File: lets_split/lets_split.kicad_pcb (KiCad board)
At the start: 2 copper layers, 113 x 82 mm, 83 parts, among them J2 CONN_01X04, P1 USB-rewire, P2 USB_OTG, P3 WS2812-Strip, SW1 SW_PUSH, SW10 SW_PUSH, SW11 SW_PUSH, SW12 SW_PUSH, SW13 SW_PUSH, SW14 SW_PUSH, SW15 SW_PUSH, SW16 SW_PUSH, SW17 SW_PUSH, SW18 SW_PUSH, SW19 SW_PUSH, SW2 SW_PUSH, SW20 SW_PUSH, SW21 SW_PUSH, SW22 SW_PUSH, SW23 SW_PUSH, SW24 SW_PUSH, SW3 SW_PUSH, SW4 SW_PUSH, SW5 SW_PUSH, SW6 SW_PUSH, SW7 SW_PUSH, SW8 SW_PUSH, SW9 SW_PUSH, U1 ArduinoProMicro

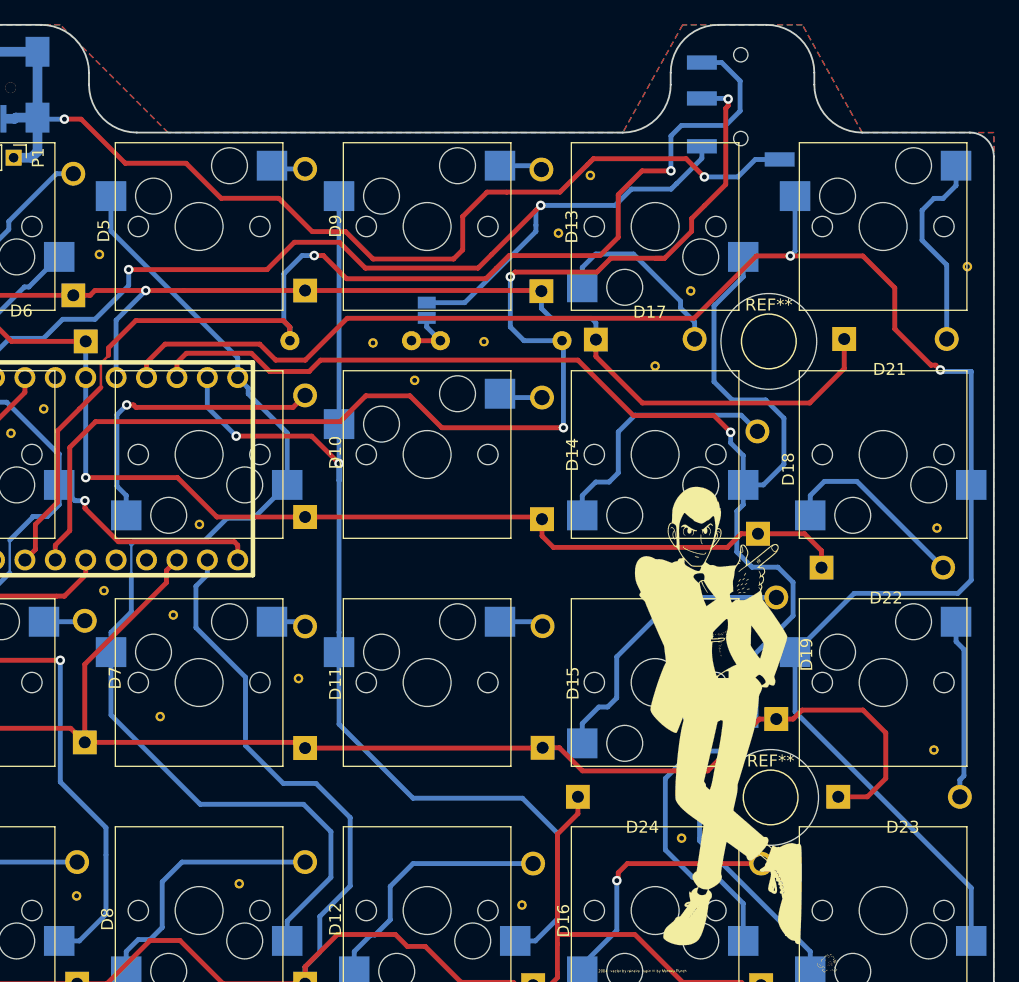
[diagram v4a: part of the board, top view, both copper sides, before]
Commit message: Changed to actually aquireable TRRS connector
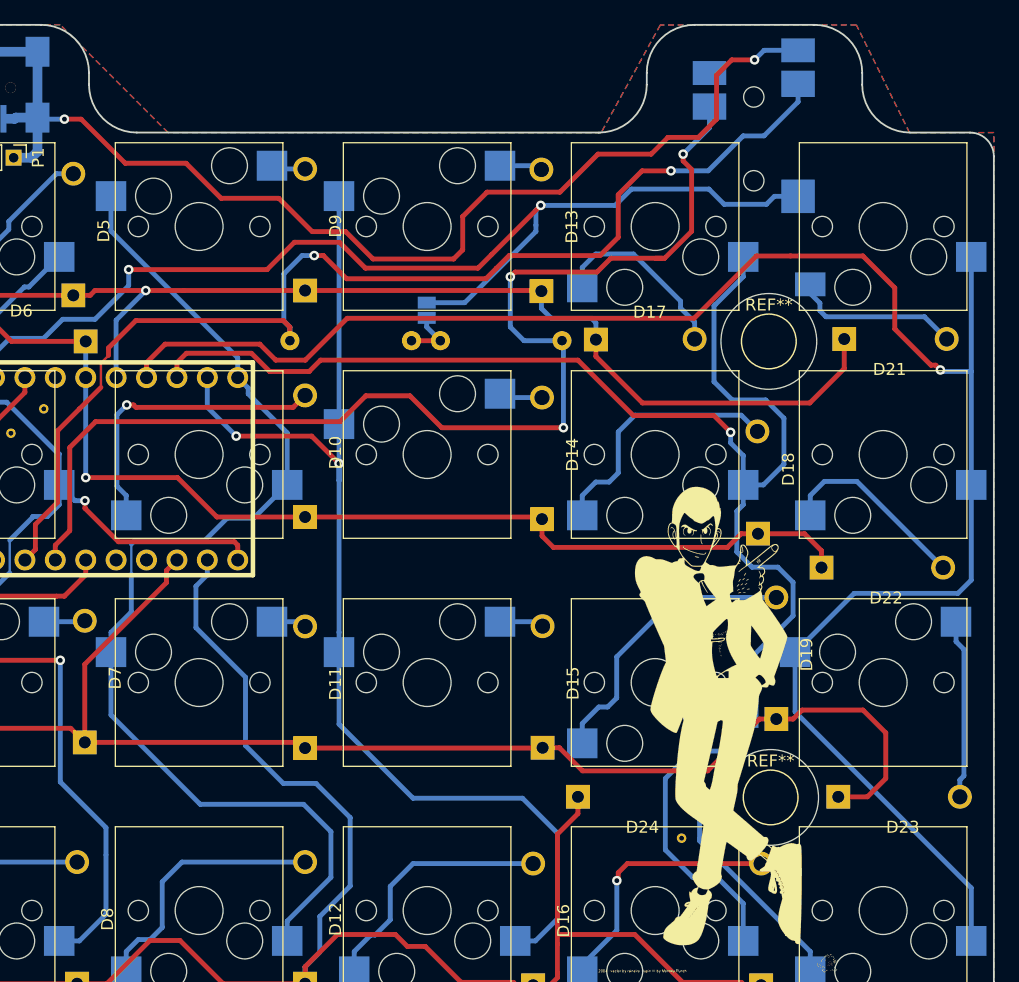
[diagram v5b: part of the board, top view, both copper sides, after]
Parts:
- removed J2: CONN_01X04, Connectors:4ucon-20153
- removed the REF** at (152.4, 82.5)
- removed the REF** at (120.3, 75.2)
- removed the REF** at (169.7, 78.2)
- removed the REF** at (158.6, 73.4)
- removed the REF** at (192.8, 76.2)
- removed the REF** at (190.2, 98.0)
- removed the REF** at (190.0, 116.6)
- removed the REF** at (155.6, 129.5)
- removed the REF** at (118.4, 128.8)
- removed the REF** at (132.0, 127.8)
- removed the REF** at (143.1, 82.6)
- removed the REF** at (125.3, 113.8)
- removed the REF** at (136.9, 110.6)
- removed the REF** at (161.3, 68.6)
- removed the REF** at (146.6, 85.7)
- removed the REF** at (166.7, 84.5)
- removed the REF** at (128.6, 97.7)
- removed the REF** at (120.7, 103.3)
- removed the REF** at (126.4, 105.3)
- added P4: TRRS jack, Connectors:SJ-4351X-SMT, B.Cu at (174.9, 65.3)
- turned SW6 to 180 degrees
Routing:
- net VCC: track 128.5 -> 135.3 mm
- net GND: track 137.2 -> 143.4 mm
- net col5: track 151.0 -> 155.4 mm, vias 2 -> 1
- net Net-(D21-Pad2): track 17.0 -> 13.9 mm
- net SCL/D3: track 102.1 -> 99.2 mm
- net SDA: track 99.4 -> 98.0 mm
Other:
- outline, holes or cut-outs redrawn
